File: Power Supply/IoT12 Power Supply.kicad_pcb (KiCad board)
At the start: 2 copper layers, 91.4 x 73.7 mm, 16 parts, among them J1 Screw_Terminal_01x03, J2 Screw_Terminal_01x03

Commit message: Changed license to permissive.
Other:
- board text added: "Recommended power supply module: Mean Well MPM-90-24 Input: 80-264VAC, 113-370VDC. Output: 24V, 3.75A, 90W. Lower power alternatives: Mean Well MPM-30-15 Input: 80-264VAC. Output: 15V, 2.3A, 30W. Mean Well MPM-20-12 Input: 80-264VAC, 113V-370VDC. Output: 12V, 1.8A, 21.6W. https://github.com/atoomnetmarc/IoT12-hardware Apache License, Version 2.0"
- board text removed: "Recommended power supply module: Mean Well MPM-90-24 Input: 80-264VAC, 113-370VDC. Output: 24V, 3.75A, 90W. Lower power alternatives: Mean Well MPM-30-15 Input: 80-264VAC. Output: 15V, 2.3A, 30W. Mean Well MPM-20-12 Input: 80-264VAC, 113V-370VDC. Output: 12V, 1.8A, 21.6W. https://github.com/atoomnetmarc/IoT12-hardware License: Creative Commons Attribution-NonCommercial 3.0 Unported"

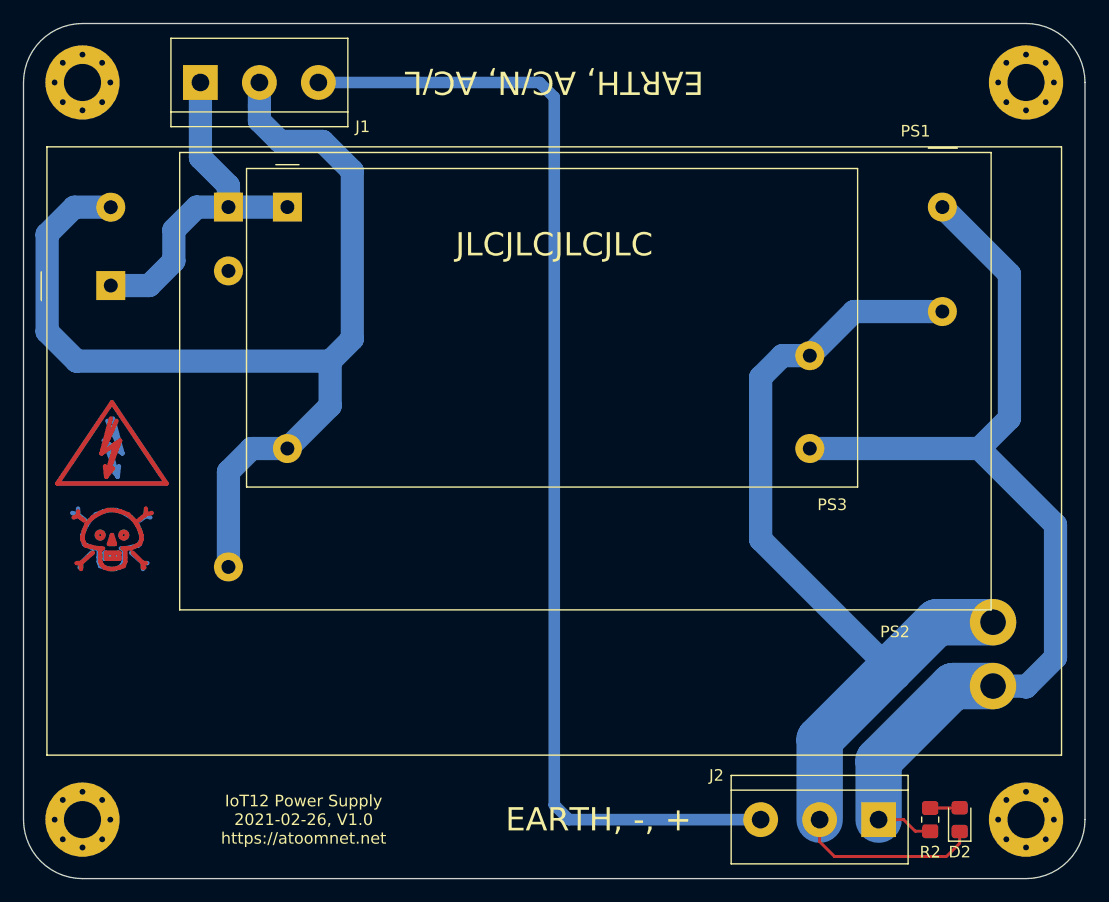
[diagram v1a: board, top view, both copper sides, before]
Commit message: Rotated J1, J2.
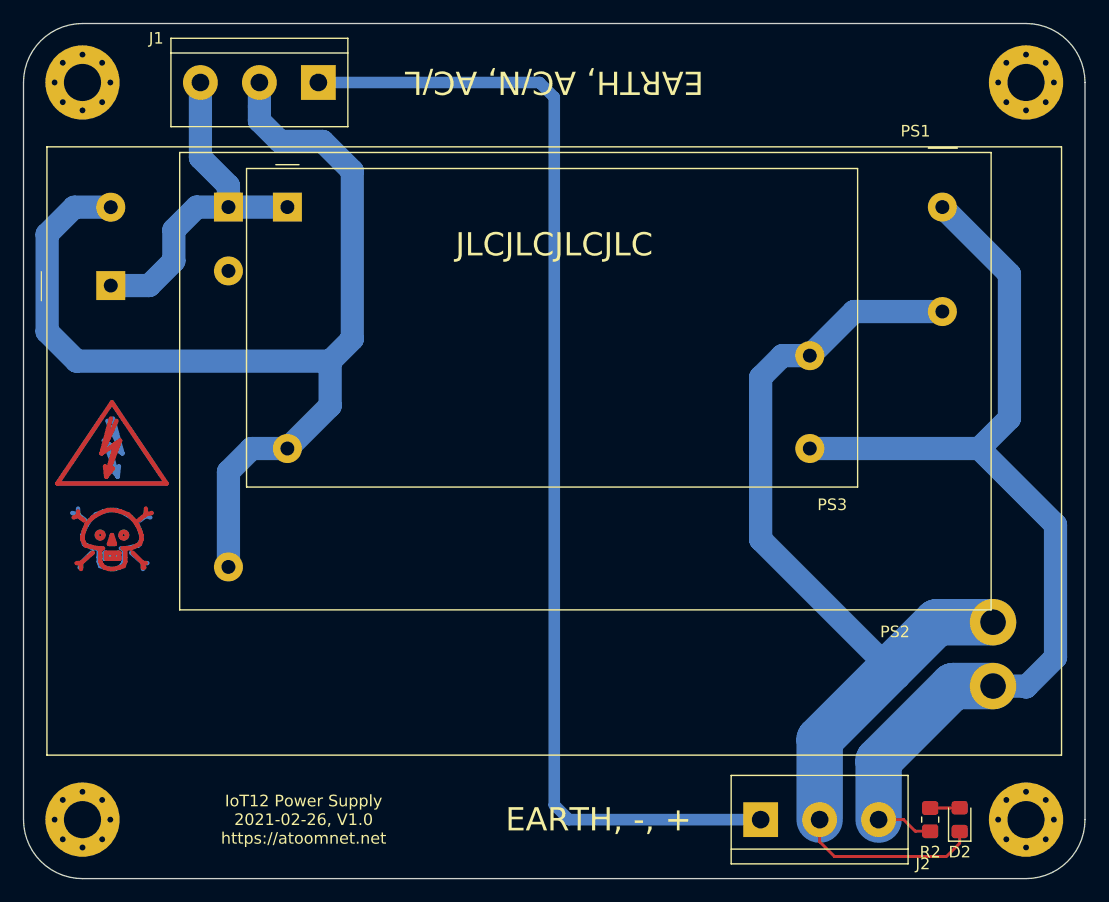
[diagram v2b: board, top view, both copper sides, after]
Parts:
- moved J1 10.2 mm to (132.1, 58.4), turned to 180 degrees
- moved J2 10.2 mm to (170.2, 121.9), turned to 0 degrees
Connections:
- J1 pad 1: /L -> Earth
- J1 pad 3: Earth -> /L
- J2 pad 1: /Vout+ -> Earth
- J2 pad 3: Earth -> /Vout+

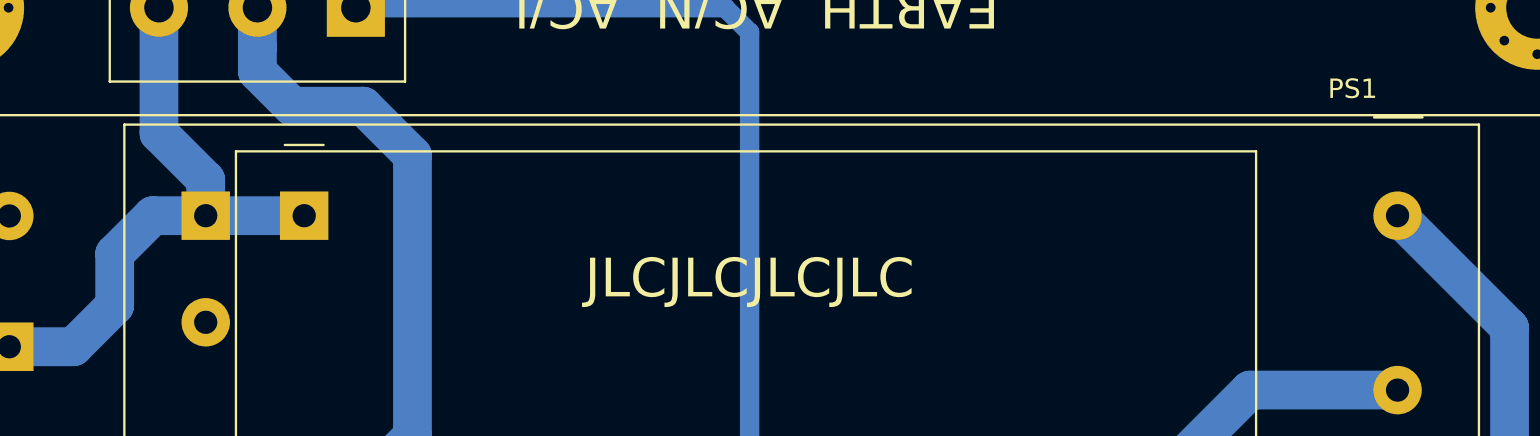
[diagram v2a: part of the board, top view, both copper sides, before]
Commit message: Updated pin1 marker of PS2.
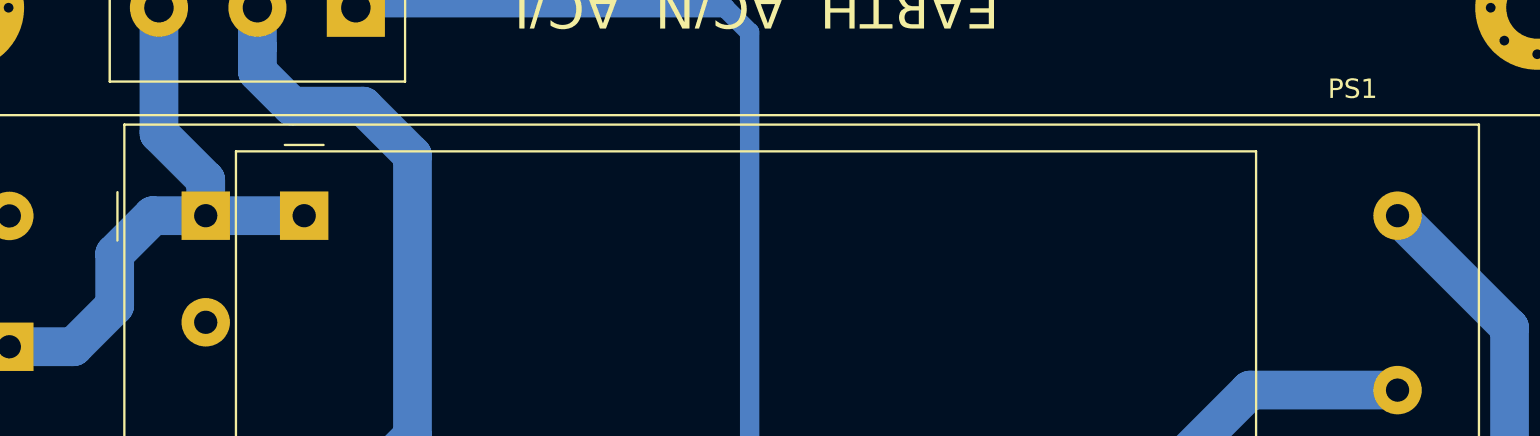
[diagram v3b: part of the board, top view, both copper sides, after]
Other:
- board text removed: "JLCJLCJLCJLC"
